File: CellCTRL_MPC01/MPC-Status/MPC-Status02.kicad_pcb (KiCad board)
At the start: 4 copper layers, 70 x 70 mm, 35 parts, among them J1 Programming, J2 I2C, J3 Reset, U1 ATtiny202-SS

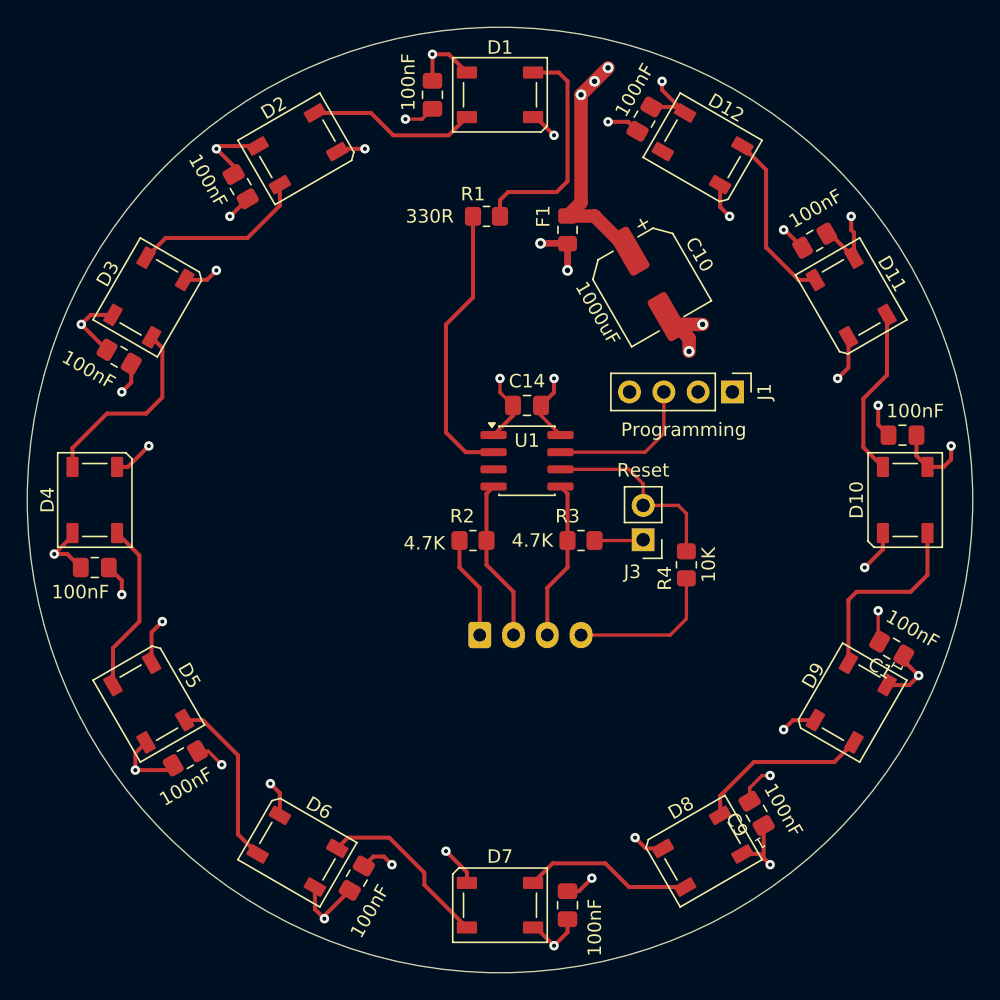
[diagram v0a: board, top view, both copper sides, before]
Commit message: Update der PCBs
MPC01: Update der Schematics (Lötbrücken anstatt von Steckbrücken bei MSN und generell Brücken bei PDNUart)
MPC-Status: Fertigstellen des PCBs
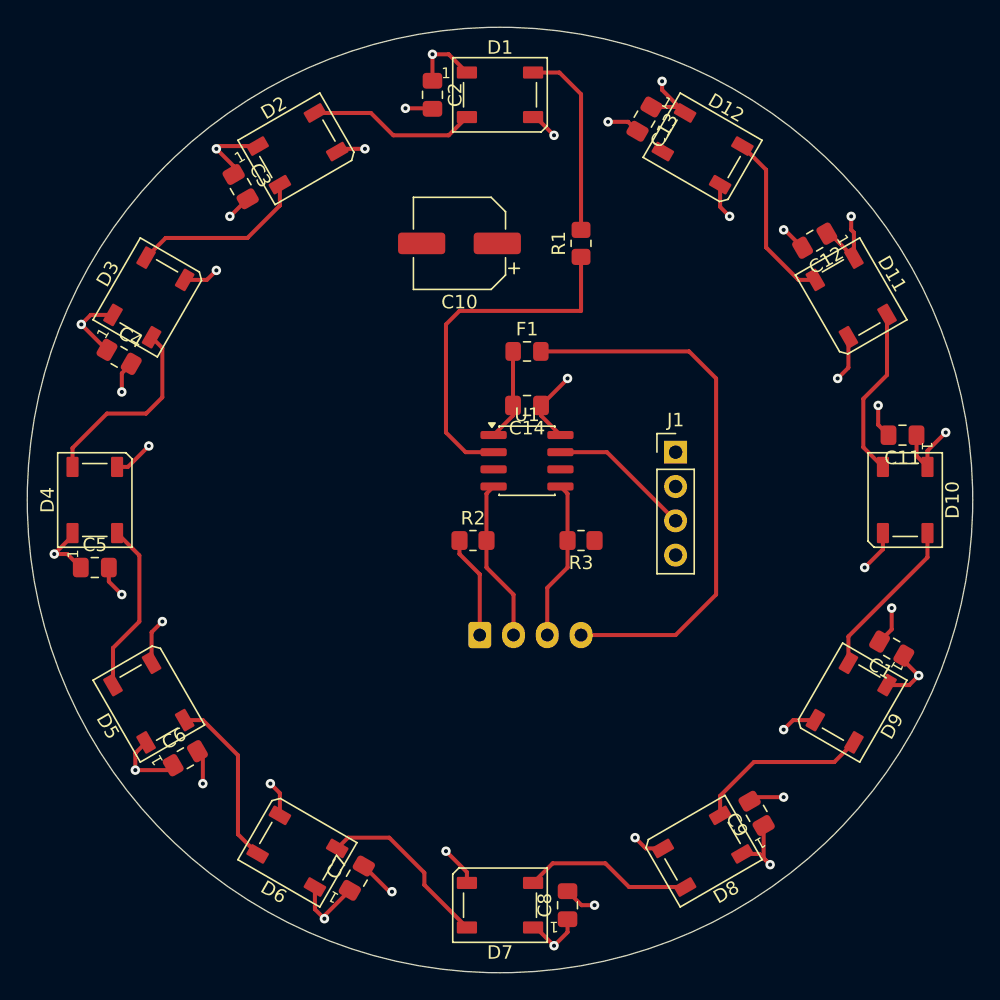
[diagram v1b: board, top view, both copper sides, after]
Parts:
- removed J3: Reset, Connector_PinHeader_2.54mm:PinHeader_1x02_P2.54mm_Vertical
- removed R4: 10K, Resistor_SMD:R_0805_2012Metric_Pad1.20x1.40mm_HandSolder
- moved C10 14.3 mm to (147.0, 86.0), turned to 180 degrees
- moved F1 9.49 mm to (152.0, 94.0), turned to 0 degrees
- moved R1 7.28 mm to (156.0, 86.0), turned to 90 degrees
- moved J1 6.13 mm to (163.0, 101.5), turned to 0 degrees
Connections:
- C1 pad 1: +5VD -> +5V
- C10 pad 1: +5VD -> +5V
- C11 pad 1: +5VD -> +5V
- C12 pad 1: +5VD -> +5V
- C13 pad 1: +5VD -> +5V
- C2 pad 1: +5VD -> +5V
- C3 pad 1: +5VD -> +5V
- C4 pad 1: +5VD -> +5V
- C5 pad 1: +5VD -> +5V
- C6 pad 1: +5VD -> +5V
- C7 pad 1: +5VD -> +5V
- C8 pad 1: +5VD -> +5V
- C9 pad 1: +5VD -> +5V
- D1 pad 1: +5VD -> +5V
- D10 pad 1: +5VD -> +5V
- D11 pad 1: +5VD -> +5V
- D12 pad 1: +5VD -> +5V
- D2 pad 1: +5VD -> +5V
- D3 pad 1: +5VD -> +5V
- D4 pad 1: +5VD -> +5V
- D5 pad 1: +5VD -> +5V
- D6 pad 1: +5VD -> +5V
- D7 pad 1: +5VD -> +5V
- D8 pad 1: +5VD -> +5V
- D9 pad 1: +5VD -> +5V
- F1 pad 1: +5VD -> +5V
- F1 pad 2: +5V -> Net-(J2-Pin_4)
- J1 pad 1: GND -> unconnected-(J1-Pin_1-Pad1)
- J1 pad 2: unconnected-(J1-Pin_2-Pad2) -> GND
- J2 pad 4: +5V -> Net-(J2-Pin_4)
- U1 pad 6: Reset -> unconnected-(U1-~{RESET}/PA0-Pad6)
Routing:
- net +5VD: track 81.0 -> 0.00 mm, vias 15 -> 0
- net +5V: track 20.5 -> 70.0 mm, vias 3 -> 12
- net Net-(J2-Pin_4): track 0.00 -> 41.0 mm
- net Reset: track 14.4 -> 0.00 mm
- net GND: track 88.8 -> 75.2 mm, vias 27 -> 25
- net Neopixel_DATA: track 21.0 -> 26.5 mm
- net Net-(D1-DIN): track 17.0 -> 14.3 mm
- net DOUT/IN: track 14.4 -> 12.0 mm
- net Programmierpin: track 11.3 -> 10.6 mm
- removed copper zone on In2.Cu, net +5VD
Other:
- board text removed: "100nF"
- board text removed: "I2C"
